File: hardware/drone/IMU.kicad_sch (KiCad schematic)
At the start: 0 parts

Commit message: save before axing motor driver ic's
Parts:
- added C23, C24: u1, SamacSys_Parts:MAJx16, symbol Device:C
- added C25: 0u1, symbol Device:C
- added C26: 4u7, symbol Device:C
- added IC4: LPS25HBTR, LPS25HBTR, symbol SamacSys_Parts:LPS25HBTR
- added IC5: BMI323, SamacSys_Parts:BMI323, symbol SamacSys_Parts:BMI323
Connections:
- new net +3V3: C23.1, C24.1, C25.1, C26.1, IC4.1 (VDD_IO), IC4.10 (VDD), IC5.5 (VDDIO), IC5.8 (VDD)
- new net BARO.CS: IC4.6 (CS)
- new net BARO.INT: IC4.7 (INT_DRDY)
- new net GND: C23.2, C24.2, C25.2, C26.2, IC4.3 (RES), IC4.8 (GND_1), IC4.9 (GND_2), IC5.6 (GNDIO), IC5.7 (GND)
- new net IMU.INT1: IC5.4 (INT1)
- new net IMU.INT2: IC5.9 (INT2)
- new net IMU_CS: IC5.12 (CSB)
- new net SPI.MISO: IC4.5 (SDO/_SA0), IC5.1 (SDO/MISO)
- new net SPI.MOSI: IC4.4 (SDA/SDI/SDO), IC5.14 (SDX/MOSI)
- new net SPI.SCK: IC4.2 (SCL/_SPC), IC5.13 (SCX)
- no-connect marks 0 -> 4
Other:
- note added: "Baromter"
- note added: "Hierarchical Labels"
- note added: "Inertial Measurement Unit (IMU)"

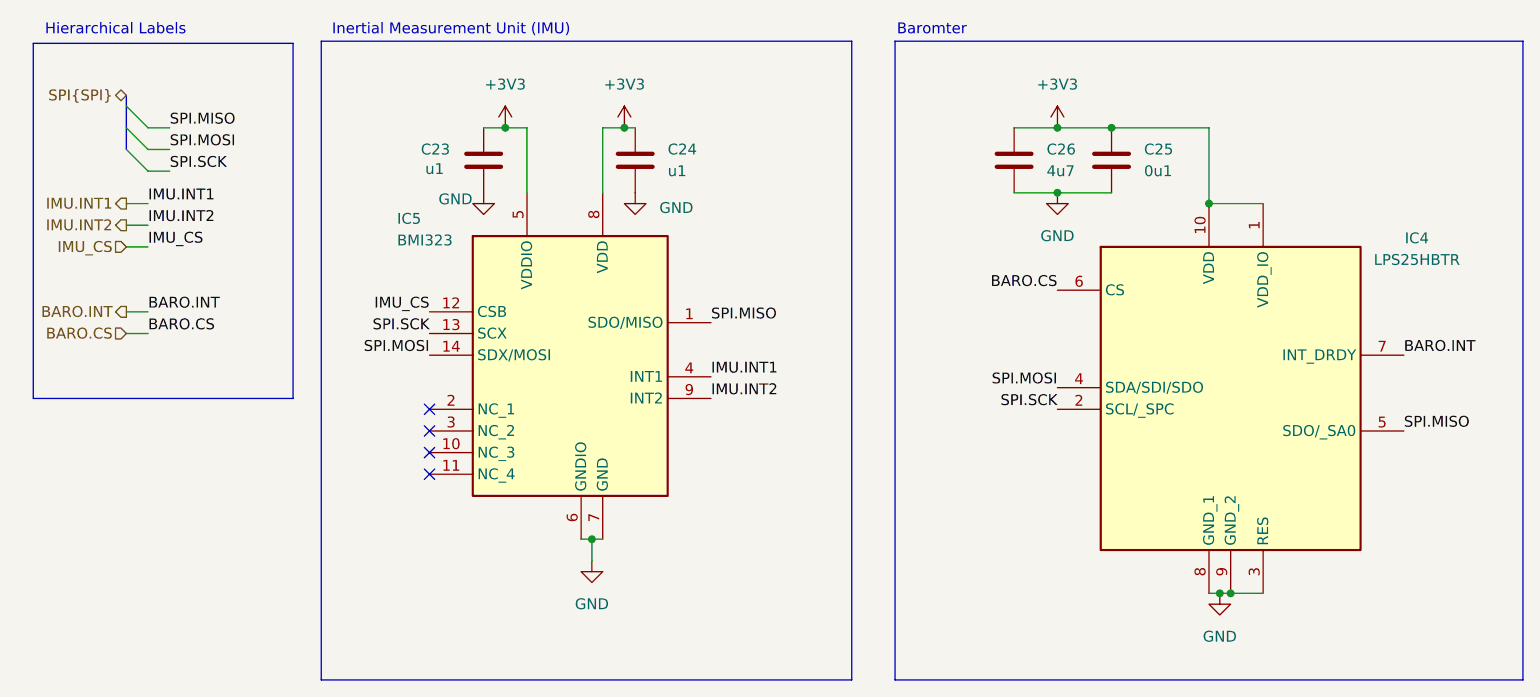
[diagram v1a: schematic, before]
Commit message: axed motor drivers. finished layout for drone but need to review overall system design after reading some stuff
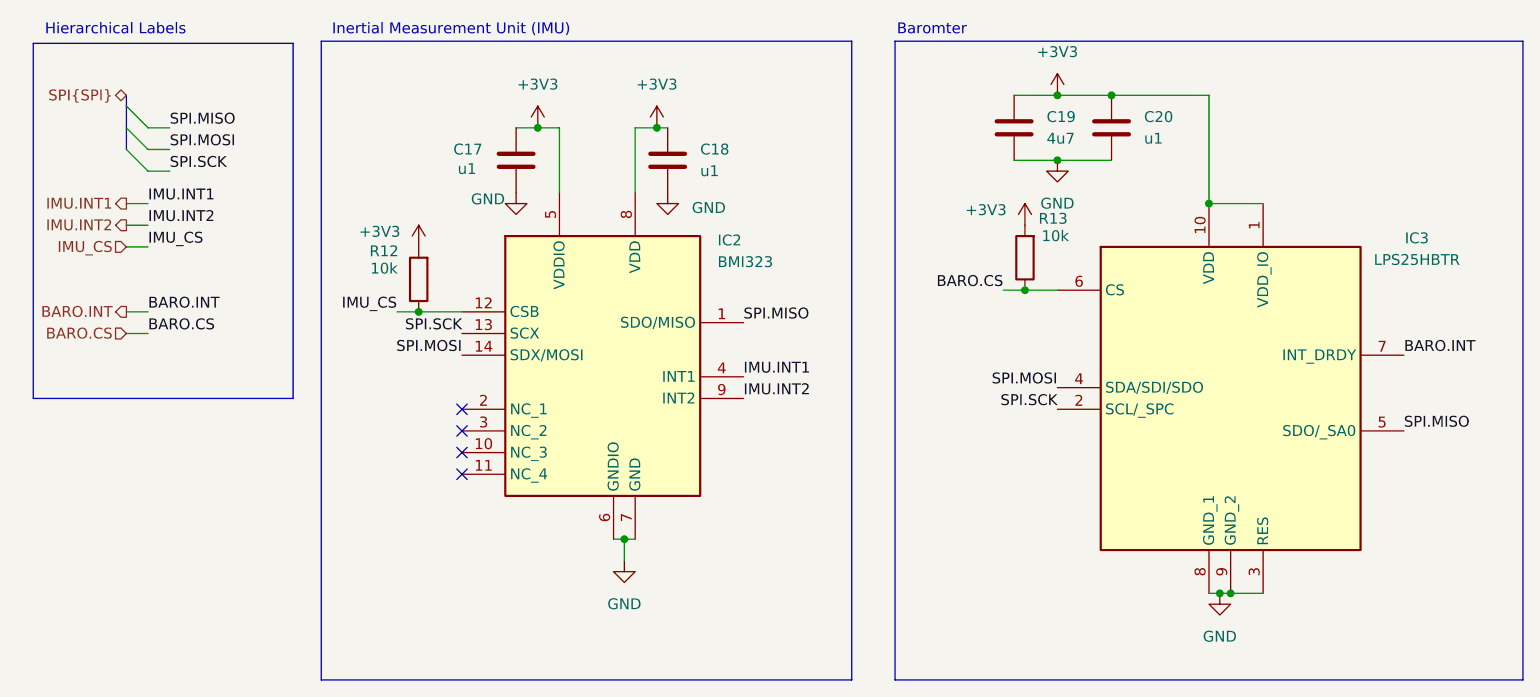
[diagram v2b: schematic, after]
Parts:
- removed C25: 0u1, symbol Device:C
- added C20: u1, SamacSys_Parts:MAJx16, symbol Device:C
- added R12, R13: 10k, SamacSys_Parts:RESC2012X60N, symbol Device:R
- C19: renamed from C26; footprint (none) -> SamacSys_Parts:CAPC1608X90N; Height (none) -> 0.9; Manufacturer_Name (none) -> TAIYO YUDEN; Manufacturer_Part_Number (none) -> AMK107BJ475MA-T
- IC3: renamed from IC4; footprint LPS25HBTR -> SamacSys_Parts:LPS25HBTR
- renumbered C23 to C17, C24 to C18, IC5 to IC2
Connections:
- net +3V3: now also C20.1, R12.2, R13.2
- net BARO.CS: now also R13.1
- net GND: now also C20.2
- net IMU_CS: now also R12.1
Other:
- moved on the sheet: C17, C18, C19, IC2
